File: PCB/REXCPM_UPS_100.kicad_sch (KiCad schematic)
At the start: 7 parts, among them J1 Model_100_System_BUS, J2 Conn_01x03_Pin, U1 742G02

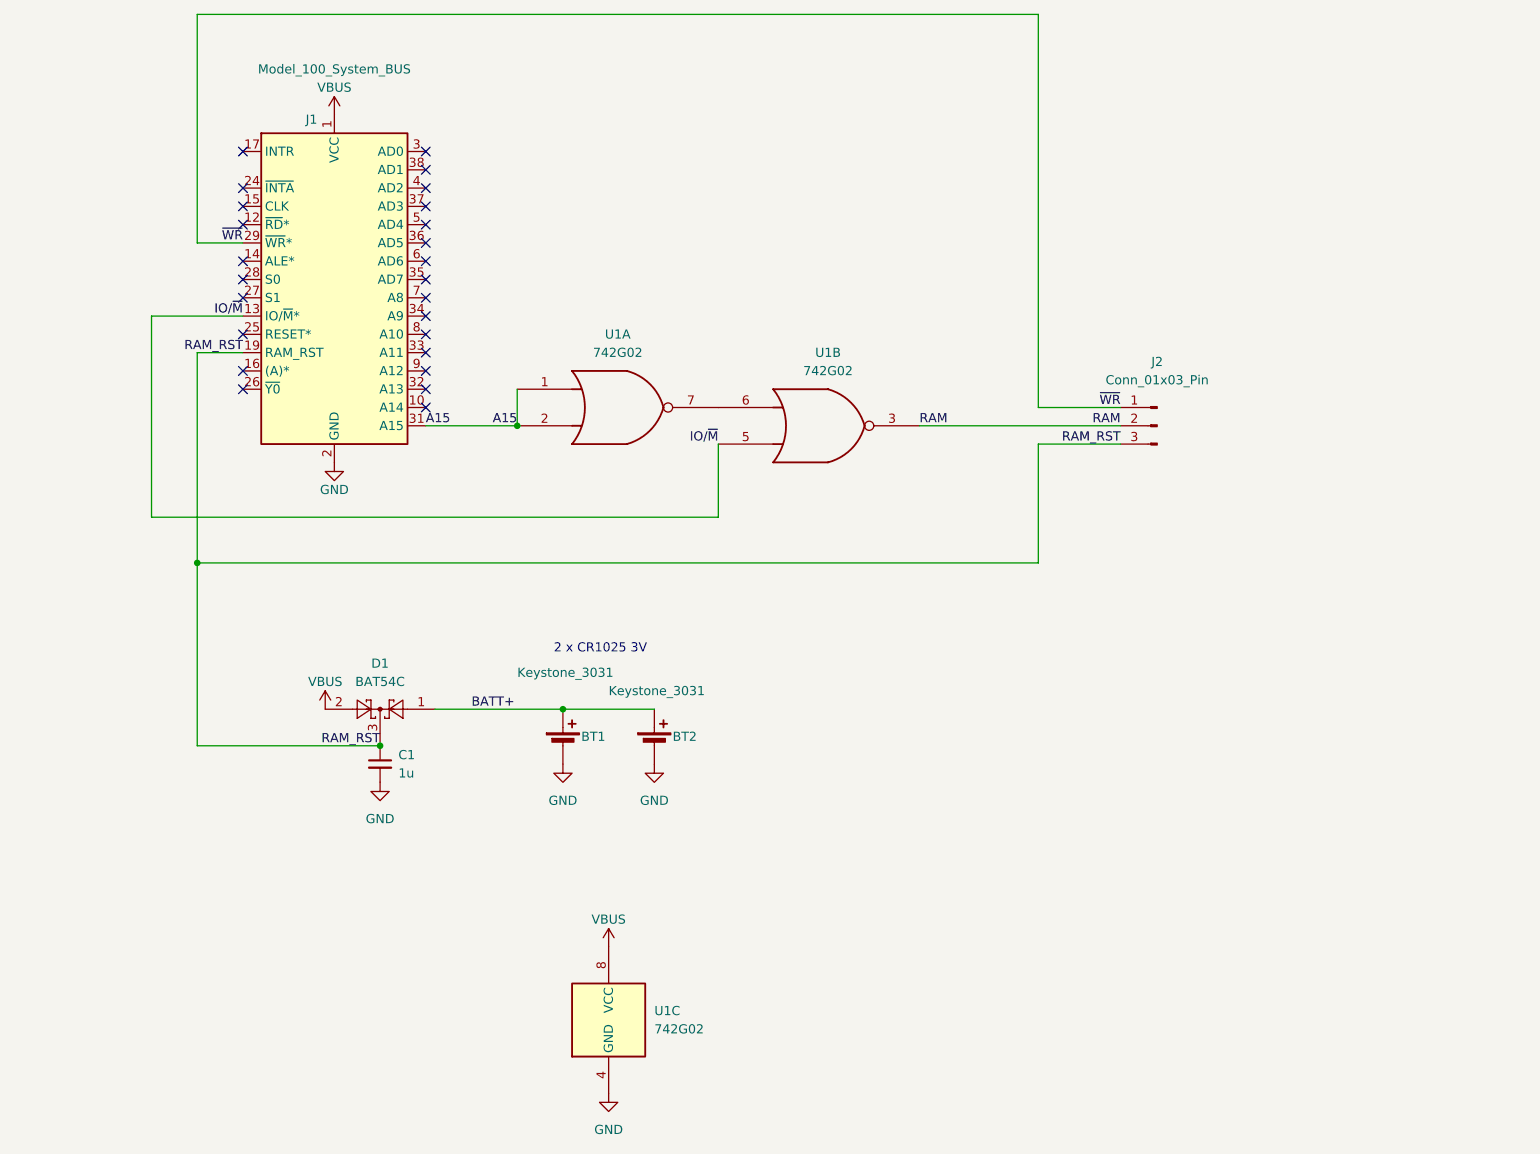
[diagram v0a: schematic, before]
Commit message: m100 4 cells & jst-sh 4 pin
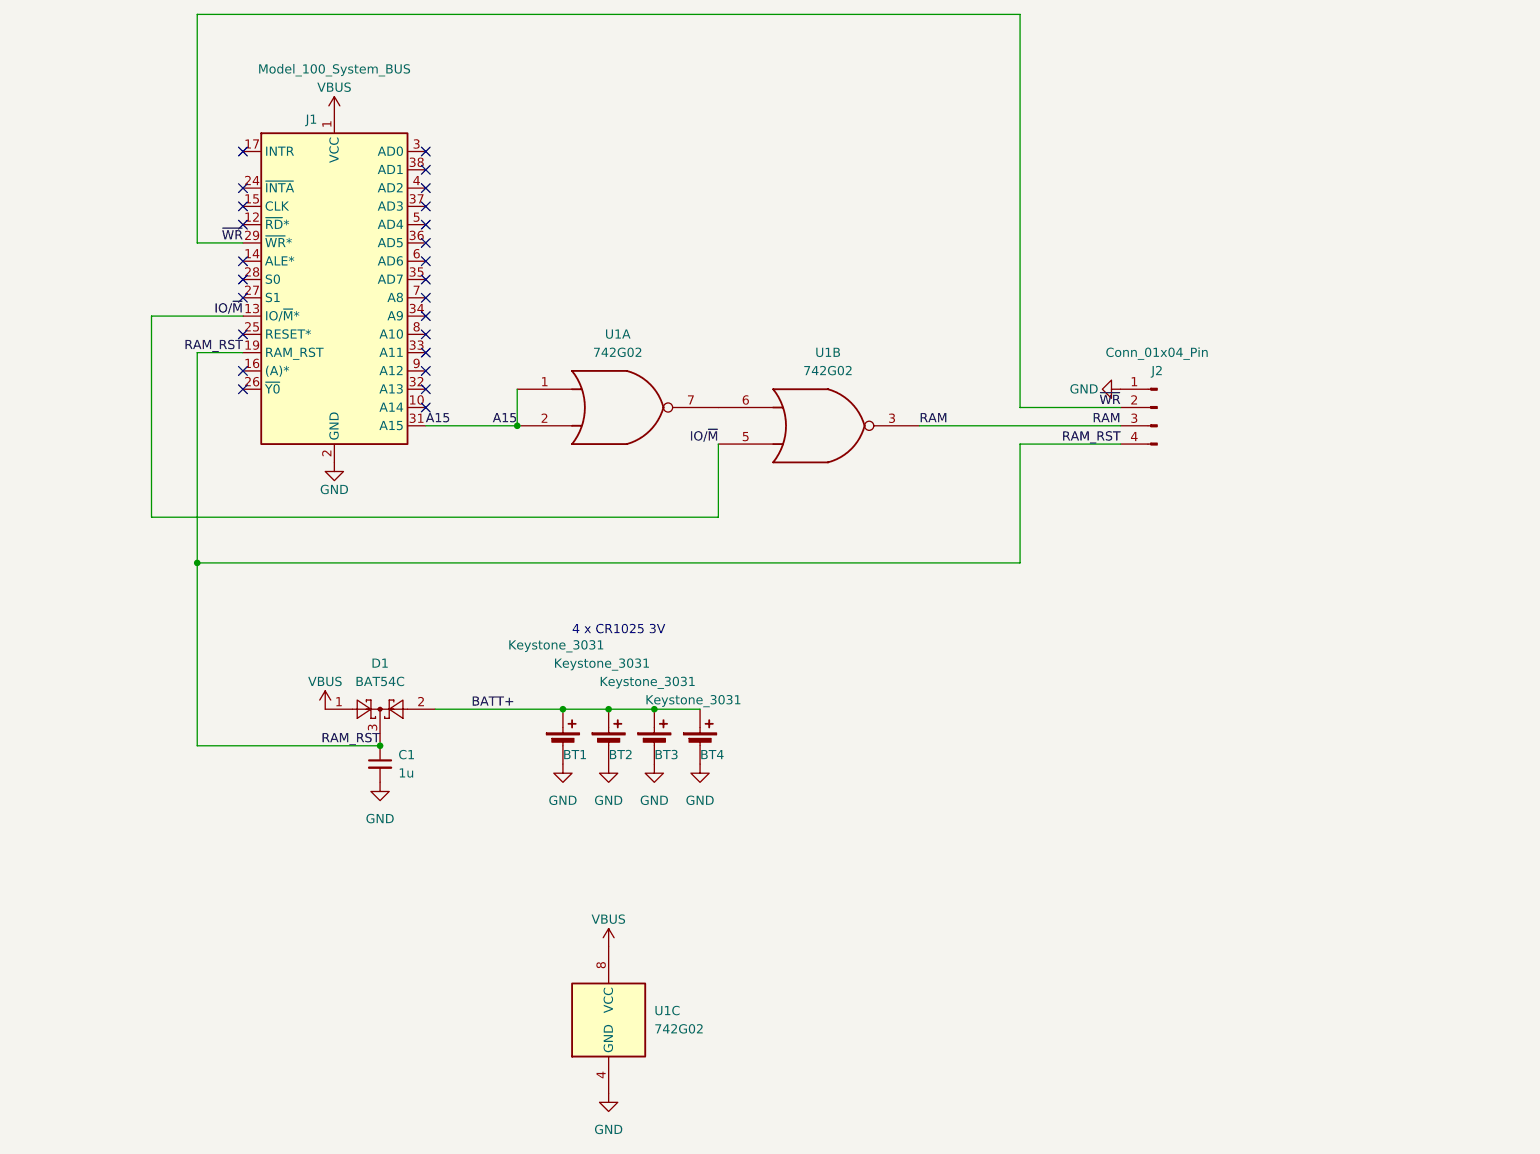
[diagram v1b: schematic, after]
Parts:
- removed J2: Conn_01x03_Pin, 000_LOCAL:PinHeader_1x03_P2.54mm_Horizontal, symbol 000_LOCAL:Conn_01x03_Pin
- added BT3, BT4: Keystone_3031, 000_LOCAL:Keystone_3031, symbol 000_LOCAL:Battery_Cell
- added J2: Conn_01x04_Pin, 000_LOCAL:JST_SH_SM04B-SRSS-TB_1x04-1MP_P1.00mm_Horizontal, symbol 000_LOCAL:Conn_01x04_Pin
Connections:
- net BATT+: now also D1.2, BT3.1 (+), BT4.1 (+); no longer D1.1
- net GND: now also BT3.2 (-), BT4.2 (-), J2.1 (Pin_1)
- net RAM: now also J2.3 (Pin_3)
- net RAM_RST: now also J2.4 (Pin_4)
- net VBUS: now also D1.1; no longer D1.2
- net ~{WR}: now also J2.2 (Pin_2)
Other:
- note added: "4 x CR1025 3V"
- note removed: "2 x CR1025 3V"
- moved on the sheet: BT2

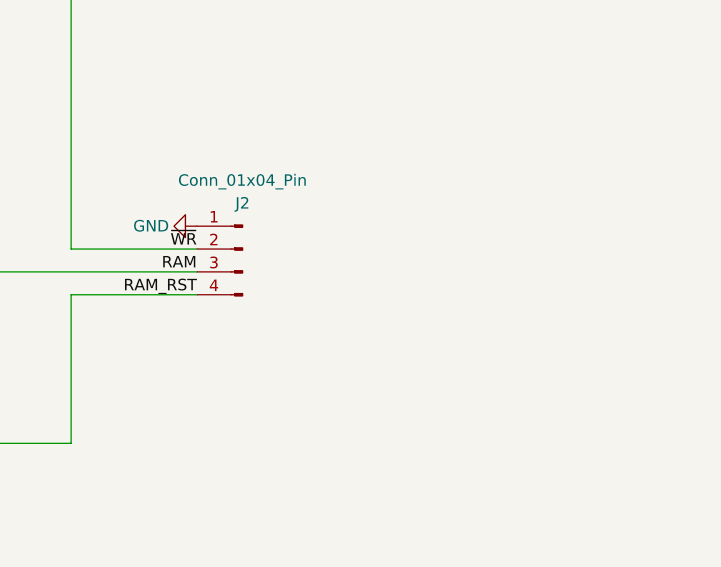
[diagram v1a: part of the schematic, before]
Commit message: 4-cells, add gnd wire, jst-sh connector
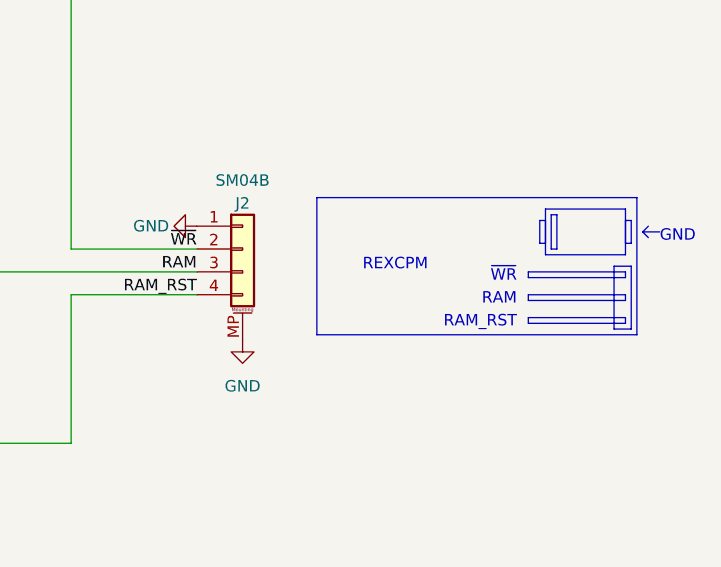
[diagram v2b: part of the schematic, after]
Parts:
- J2: value Conn_01x04_Pin -> SM04B; symbol 000_LOCAL:Conn_01x04_Pin -> 000_LOCAL:Conn_01x04_MountingPin
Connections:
- net GND: now also J2.MP (MountPin)
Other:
- note added: "GND"
- note added: "RAM"
- note added: "RAM_RST"
- note added: "REXCPM"
- note added: "~{WR}"
- title: REXCPM UPS for Model 100 -> REXCPM_UPS_100
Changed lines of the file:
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@@
   (paper "USLetter")
   (title_block
-    (title "REXCPM UPS for Model 100")
+    (title "REXCPM_UPS_100")
     (date "2023-09-13")
     (rev "003")
@@
   (no_connect (at 107.95 72.39))
   (no_connect (at 107.95 82.55))
+  (polyline (pts (xy 254.635 90.17) (xy 254 90.805))
+    (stroke (width 0) (type default))
+  )
   (wire (pts (xy 82.55 85.09) (xy 76.2 85.09))
     (stroke (width 0) (type default))
@@
     (stroke (width 0) (type default))
   )
+  (polyline (pts (xy 254 90.805) (xy 255.905 90.805))
+    (stroke (width 0) (type default))
+  )
   (wire (pts (xy 109.22 134.62) (xy 127 134.62))
     (stroke (width 0) (type default))
@@
     (stroke (width 0) (type default))
   )
+  (polyline (pts (xy 254 90.805) (xy 254.635 91.44))
+    (stroke (width 0) (type default))
+  )
   (wire (pts (xy 120.65 90.17) (xy 120.65 95.25))
     (stroke (width 0) (type default))
   )
+  (rectangle (start 241.3 97.79) (end 252.095 98.425)
+    (stroke (width 0) (type default))
+    (fill (type none))
+  )
+  (rectangle (start 243.205 88.265) (end 252.095 93.345)
+    (stroke (width 0) (type default))
+    (fill (type none))
+  )
+  (rectangle (start 243.84 88.9) (end 244.475 92.71)
+    (stroke (width 0) (type default))
+    (fill (type color) (color 0 0 0 0))
+  )
+  (rectangle (start 252.095 89.535) (end 252.73 92.075)
+    (stroke (width 0) (type default))
+    (fill (type none))
+  )
+  (rectangle (start 250.825 94.615) (end 252.73 101.6)
+    (stroke (width -0.0001) (type default))
+    (fill (type color) (color 0 0 0 0))
+  )
+  (rectangle (start 242.57 89.535) (end 243.205 92.075)
+    (stroke (width 0) (type default))
+    (fill (type none))
+  )
+  (rectangle (start 217.805 86.995) (end 253.365 102.235)
+    (stroke (width 0) (type default))
+    (fill (type none))
+  )
+  (rectangle (start 241.3 100.33) (end 252.095 100.965)
+    (stroke (width 0) (type default))
+    (fill (type none))
+  )
+  (rectangle (start 241.3 95.25) (end 252.095 95.885)
+    (stroke (width 0) (type default))
+    (fill (type none))
+  )
+  (text "~{WR}" (at 240.03 96.52 0)
+    (effects (font (size 1.27 1.27)) (justify right bottom))
+  )
+  (text "RAM" (at 240.03 99.06 0)
+    (effects (font (size 1.27 1.27)) (justify right bottom))
+  )
+  (text "GND" (at 255.905 92.075 0)
+    (effects (font (size 1.27 1.27)) (justify left bottom))
+  )
   (text "4 x CR1025 3V" (at 128.27 124.46 0)
+    (effects (font (size 1.27 1.27)) (justify left bottom))
+  )
+  (text "RAM_RST" (at 240.03 101.6 0)
+    (effects (font (size 1.27 1.27)) (justify right bottom))
+  )
+  (text "REXCPM" (at 222.885 95.25 0)
     (effects (font (size 1.27 1.27)) (justify left bottom))
   )
@@
     )
   )
-  (symbol (lib_id "000_LOCAL:Conn_01x04_Pin") (at 209.55 92.71 0) (mirror y) (unit 1)
+  (symbol (lib_id "000_LOCAL:Conn_01x04_MountingPin") (at 209.55 92.71 0) (unit 1)
     (in_bom yes) (on_board yes) (dnp no)
     (property "Reference" "J2" (at 209.55 87.63 0)
       (effects (font (size 1.27 1.27)))
     )
-    (property "Value" "Conn_01x04_Pin" (at 209.55 85.09 0)
+    (property "Value" "SM04B" (at 209.55 85.09 0)
       (effects (font (size 1.27 1.27)))
     )
@@
     (pin "3")
     (pin "4")
+    (pin "MP")
     (instances
       (project "REXCPM_UPS_100"
@@
         )
       )
+    )
+  )
+  (symbol (lib_name "GND_1") (lib_id "power:GND") (at 209.55 102.87 0) (unit 1)
+    (in_bom yes) (on_board yes) (dnp no) (fields_autoplaced)
+    (property "Reference" "#PWR07" (at 209.55 109.22 0)
+      (effects (font (size 1.27 1.27)) hide)
+    )
+    (property "Value" "GND" (at 209.55 107.95 0)
+      (effects (font (size 1.27 1.27)))
+    )
+    (property "Footprint" "" (at 209.55 102.87 0)
+      (effects (font (size 1.27 1.27)) hide)
+    )
+    (property "Datasheet" "" (at 209.55 102.87 0)
+      (effects (font (size 1.27 1.27)) hide)
+    )
+    (pin "1")
+    (instances
+      (project "REXCPM_UPS_100"
+        (path "/28a4b045-d480-4410-adb7-fa6b33984079"
+          (reference "#PWR07") (unit 1)
+        )
+      )

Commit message: tested m100 v004
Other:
- moved on the sheet: BT1, BT2, BT3, BT4, C1, D1, J1, J2, U1A, U1B

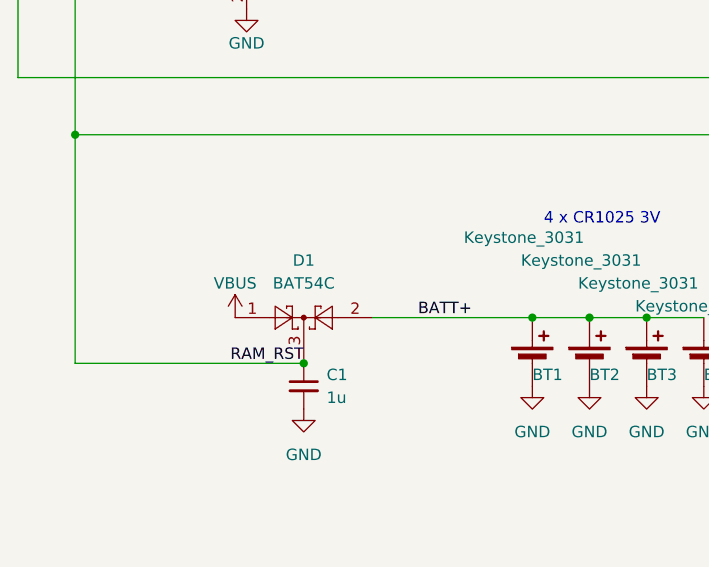
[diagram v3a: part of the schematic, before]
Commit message: replace BAT54C with BAV170 to protect batteries better
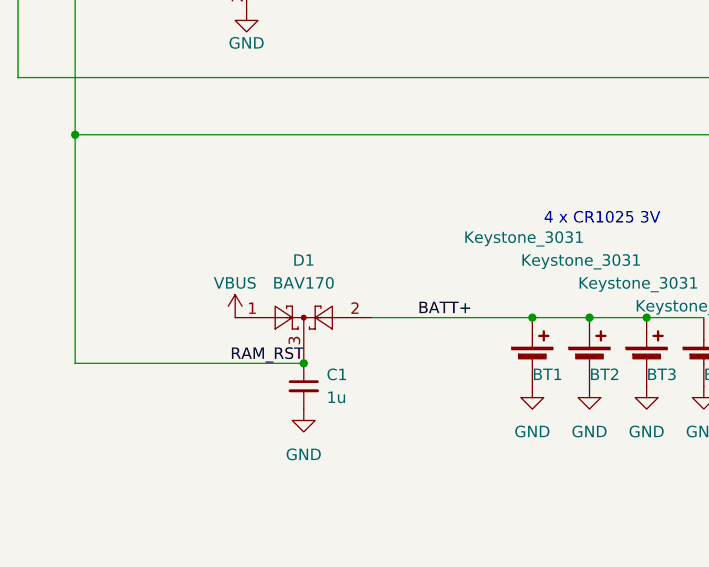
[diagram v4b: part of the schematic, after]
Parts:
- D1: value BAT54C -> BAV170
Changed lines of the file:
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@@
   (title_block
     (title "REXCPM_UPS_100")
-    (date "2023-09-13")
-    (rev "003")
+    (date "2023-09-21")
+    (rev "004")
     (company "Brian K. White - b.kenyon.w@gmail.com")
     (comment 1 "Replacement REXCPM system bus interface with memory battery")
@@
       (effects (font (size 1.27 1.27)))
     )
-    (property "Value" "BAT54C" (at 82.55 137.16 0)
+    (property "Value" "BAV170" (at 82.55 137.16 0)
       (effects (font (size 1.27 1.27)))
     )
@@
       (effects (font (size 1.27 1.27)) (justify left) hide)
     )
-    (property "Datasheet" "datasheets/BAT54C.pdf" (at 80.518 140.97 0)
-      (effects (font (size 1.27 1.27)) hide)
-    )
+    (property "Datasheet" "datasheets/BAV170.pdf" (at 80.518 140.97 0)
+      (effects (font (size 1.27 1.27)) hide)
+    )

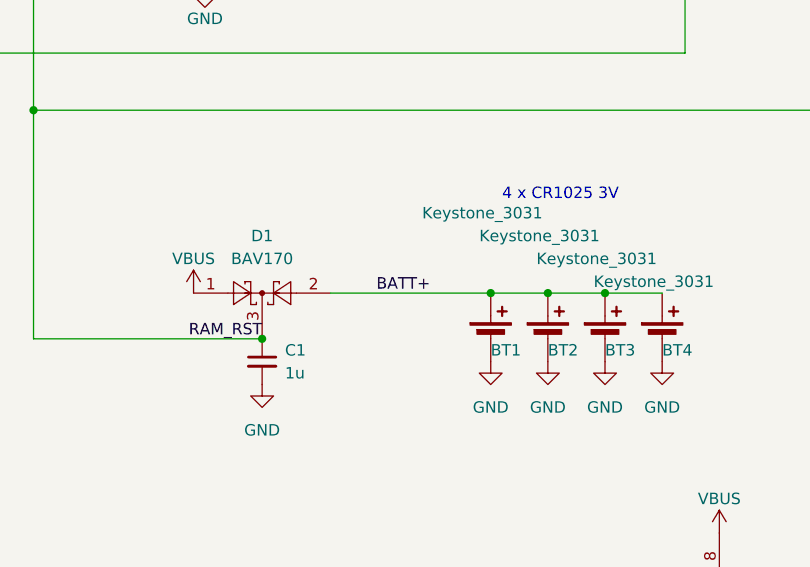
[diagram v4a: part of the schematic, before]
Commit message: m100 pcb routing, gnd, fiducials
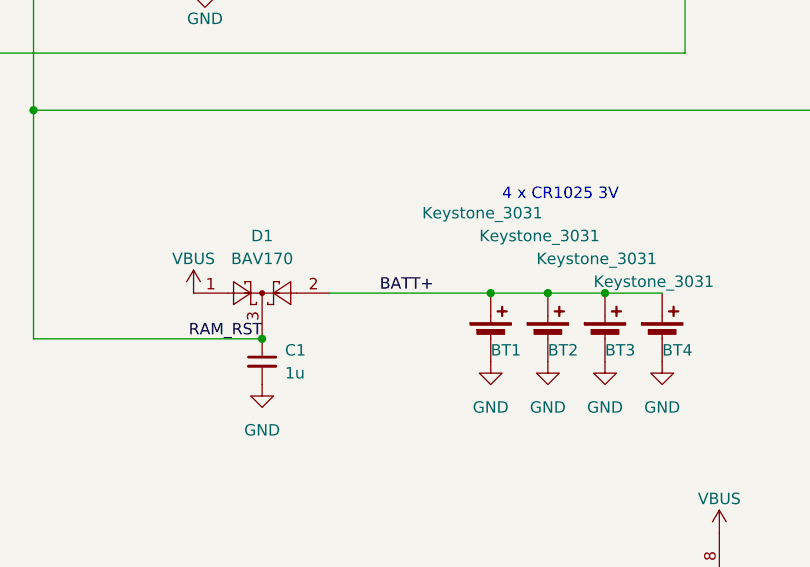
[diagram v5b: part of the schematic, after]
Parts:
- D1: footprint Package_TO_SOT_SMD:SOT-23 -> 000_LOCAL:SOT-23
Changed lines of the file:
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@@
+    (stroke (width 0) (type default))
+  )
+  (wire (pts (xy 57.15 76.2) (xy 57.15 44.45))
+    (stroke (width 0) (type default))
+  )
+  (wire (pts (xy 57.15 91.44) (xy 57.15 120.65))
+    (stroke (width 0) (type default))
+  )
+  (wire (pts (xy 120.65 140.97) (xy 127 140.97))
+    (stroke (width 0) (type default))
+  )
+  (wire (pts (xy 57.15 120.65) (xy 57.15 146.05))
+    (stroke (width 0) (type default))
+  )
+  (wire (pts (xy 129.54 104.14) (xy 129.54 114.3))
+    (stroke (width 0) (type default))
+  )
+  (wire (pts (xy 157.48 101.6) (xy 185.42 101.6))
+    (stroke (width 0) (type default))
+  )
+  (wire (pts (xy 57.15 44.45) (xy 171.45 44.45))
+    (stroke (width 0) (type default))
+  )
+  (wire (pts (xy 50.8 86.36) (xy 50.8 114.3))
+    (stroke (width 0) (type default))
+  )
+  (wire (pts (xy 63.5 76.2) (xy 57.15 76.2))
+    (stroke (width 0) (type default))
+  )
+  (wire (pts (xy 171.45 44.45) (xy 171.45 99.06))
+    (stroke (width 0) (type default))
+  )
+  (wire (pts (xy 114.3 140.97) (xy 120.65 140.97))
+    (stroke (width 0) (type default))
+  )
+  (wire (pts (xy 171.45 99.06) (xy 185.42 99.06))
+    (stroke (width 0) (type default))
+  )
+  (wire (pts (xy 63.5 86.36) (xy 50.8 86.36))
+    (stroke (width 0) (type default))
+  )
+  (wire (pts (xy 171.45 104.14) (xy 185.42 104.14))
+    (stroke (width 0) (type default))
+  )
+  (wire (pts (xy 88.9 101.6) (xy 101.6 101.6))
     (stroke (width 0) (type default))
   )
@@
     (stroke (width 0) (type default))
   )
-  (wire (pts (xy 57.15 76.2) (xy 57.15 44.45))
-    (stroke (width 0) (type default))
-  )
-  (wire (pts (xy 57.15 91.44) (xy 57.15 120.65))
-    (stroke (width 0) (type default))
-  )
-  (wire (pts (xy 120.65 140.97) (xy 127 140.97))
-    (stroke (width 0) (type default))
-  )
-  (wire (pts (xy 57.15 120.65) (xy 57.15 146.05))
-    (stroke (width 0) (type default))
-  )
-  (wire (pts (xy 129.54 104.14) (xy 129.54 114.3))
-    (stroke (width 0) (type default))
-  )
-  (wire (pts (xy 157.48 101.6) (xy 185.42 101.6))
-    (stroke (width 0) (type default))
-  )
-  (wire (pts (xy 57.15 44.45) (xy 171.45 44.45))
-    (stroke (width 0) (type default))
-  )
-  (wire (pts (xy 50.8 86.36) (xy 50.8 114.3))
-    (stroke (width 0) (type default))
-  )
-  (wire (pts (xy 63.5 76.2) (xy 57.15 76.2))
-    (stroke (width 0) (type default))
-  )
-  (wire (pts (xy 171.45 44.45) (xy 171.45 99.06))
-    (stroke (width 0) (type default))
-  )
-  (wire (pts (xy 114.3 140.97) (xy 120.65 140.97))
-    (stroke (width 0) (type default))
-  )
-  (wire (pts (xy 171.45 99.06) (xy 185.42 99.06))
-    (stroke (width 0) (type default))
-  )
-  (wire (pts (xy 63.5 86.36) (xy 50.8 86.36))
-    (stroke (width 0) (type default))
-  )
-  (wire (pts (xy 171.45 104.14) (xy 185.42 104.14))
-    (stroke (width 0) (type default))
-  )
-  (wire (pts (xy 88.9 101.6) (xy 101.6 101.6))
+  (polyline (pts (xy 236.22 96.52) (xy 236.855 97.155))
     (stroke (width 0) (type default))
   )
   (wire (pts (xy 107.95 140.97) (xy 114.3 140.97))
-    (stroke (width 0) (type default))
-  )
-  (polyline (pts (xy 236.22 96.52) (xy 236.855 97.155))
     (stroke (width 0) (type default))
   )
@@
     (effects (font (size 1.27 1.27)) (justify left bottom))
   )
-  (label "BATT+" (at 95.25 140.97 0) (fields_autoplaced)
-    (effects (font (size 1.27 1.27)) (justify left bottom))
+  (label "BATT+" (at 101.6 140.97 180) (fields_autoplaced)
+    (effects (font (size 1.27 1.27)) (justify right bottom))
   )
   (label "RAM_RST" (at 185.42 104.14 180) (fields_autoplaced)
@@
       (effects (font (size 1.27 1.27)))
     )
-    (property "Footprint" "Package_TO_SOT_SMD:SOT-23" (at 84.455 137.795 0)
+    (property "Footprint" "000_LOCAL:SOT-23" (at 84.455 137.795 0)
       (effects (font (size 1.27 1.27)) (justify left) hide)
     )
